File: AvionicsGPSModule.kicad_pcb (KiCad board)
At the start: 4 copper layers, 60 x 56.1 mm, 45 parts, among them P1 MC311D, Q1 AO3400A, Q2 AO3400A, U1 RP2040, U2 AP2112K-3.3, U3 L80-R, U4 W25Q128JVS, X1 ABM8-272-T3

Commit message: added CAN Transciever
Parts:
- added C16: 100nF, PCM_JLCPCB:C_0402, F.Cu at (130.6, 93.9)
- added R10: 1k, Resistor_SMD:R_0402_1005Metric, F.Cu at (128.7, 103.6)
- added R14: 120Ω, PCM_JLCPCB:R_0402, F.Cu at (130.5, 103.2)
- added R9: 1k, Resistor_SMD:R_0402_1005Metric, F.Cu at (126.5, 101.6)
- added U5: SN65HVD230DR, PCM_JLCPCB:SOIC-8_L4.9-W3.9-P1.27-LS6.0-BL, F.Cu at (130.7, 98.3)
- moved G*** 1.94 mm to (121.2, 98.2)
- moved C1 1.13 mm to (142.9, 102.8)
- moved U2 1.07 mm to (143.5, 105.4)
- moved C2 1.05 mm to (144.6, 108.4)
- moved C5 0.56 mm to (143.4, 99.4), turned to -90 degrees
- moved D5 0.13 mm to (137.9, 99.1)
- moved C12 0.11 mm to (153.9, 99.6)
- moved C7 0.10 mm to (153.9, 96.0)
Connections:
- net /RX renamed /UART_RX0
- net /TX renamed /UART_TX0
- REF** pad 2: (no net) -> /CANL
- REF** pad 3: (no net) -> /CANH
- U1 pad 11: unconnected-(U1-GPIO8-Pad11) -> /UART_TX1
- U1 pad 12: unconnected-(U1-GPIO9-Pad12) -> /UART_RX1
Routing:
- net GND: track 75.5 -> 104.3 mm, vias 29 -> 33
- net /CANH: track 0.00 -> 22.1 mm
- net /CANL: track 0.00 -> 21.4 mm
- net /UART_RX1: track 0.00 -> 21.0 mm
- net /UART_TX1: track 0.00 -> 17.9 mm
- net Net-(U5-VREF): track 0.00 -> 4.02 mm
- net +3.3V: track 88.0 -> 90.3 mm, vias 5 -> 3
- net /QSPI_SS: track 19.1 -> 19.7 mm
- net +5V: track 68.2 -> 67.6 mm
- net /QSPI_SD1: track 14.7 -> 15.2 mm
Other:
- board text removed: "GPS"
- board text removed: "MCU"

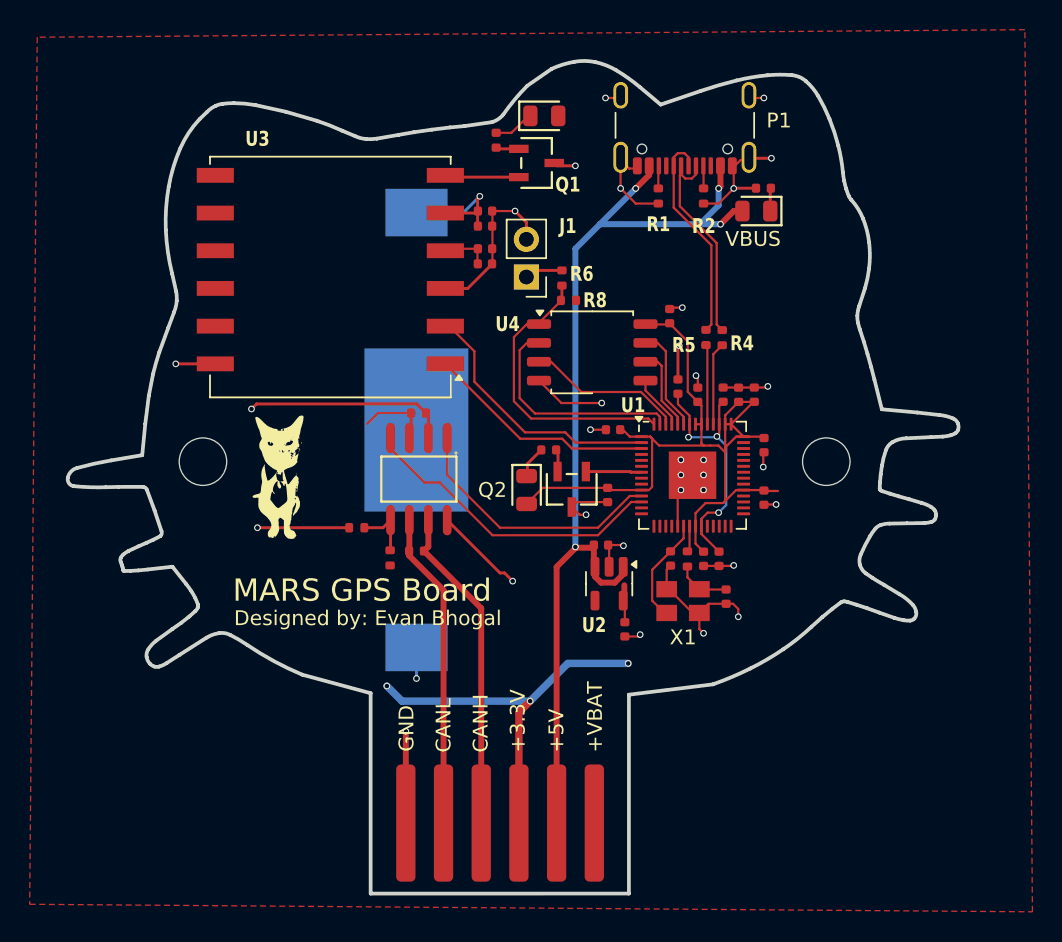
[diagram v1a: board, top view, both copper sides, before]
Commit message: Added CAN Transciever and CAN Controller
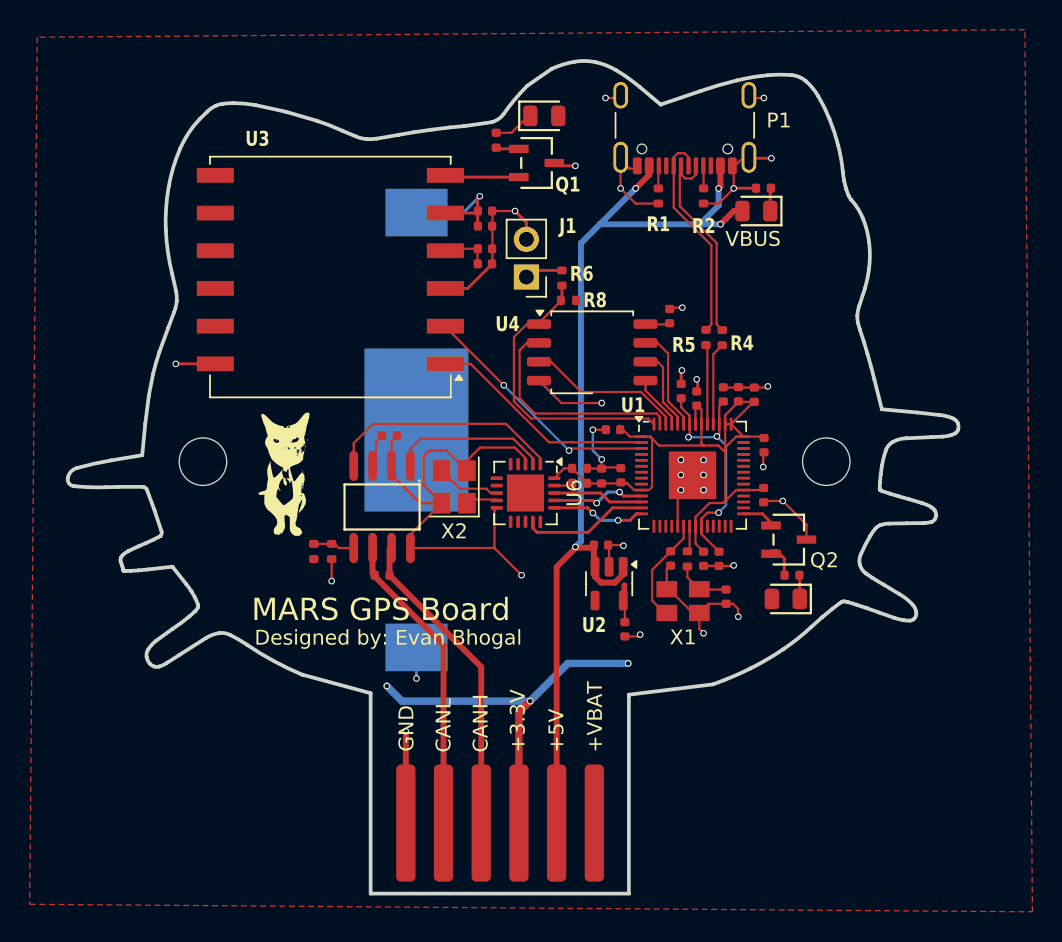
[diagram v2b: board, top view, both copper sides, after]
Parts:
- removed C4: 100n, Library:C_0402_1005Metric
- added C24: 100nF, PCM_JLCPCB:C_0402, F.Cu at (141.5, 97.6)
- added C25: 10nF, PCM_JLCPCB:C_0402, F.Cu at (143.0, 98.1)
- added C6: 100n, Library:C_0402_1005Metric, F.Cu at (151.2, 92.6)
- added R13: 5.1kΩ, PCM_JLCPCB:R_0402, F.Cu at (141.5, 98.6)
- added U6: MCP2515_I/ML, Package_DFN_QFN:QFN-20-1EP_4x4mm_P0.5mm_EP2.5x2.5mm, F.Cu at (137.9, 99.3)
- added X2: XTM32020000QT00351001, Crystal:Crystal_SMD_3225-4Pin_3.2x2.5mm, F.Cu at (133.1, 98.8)
- C11: value 100n -> 1.0u
- moved D5 18.9 mm to (155.4, 106.4), turned to 180 degrees
- moved R12 18.4 mm to (155.8, 104.8), turned to 180 degrees
- moved Q2 15.0 mm to (155.6, 102.4), turned to -90 degrees
- moved C5 11.1 mm to (152.2, 92.6), turned to 90 degrees
- moved C10 9.61 mm to (144.3, 98.1)
- moved R10 5.16 mm to (123.6, 103.2)
- moved U5 3.11 mm to (128.2, 100.2)
- moved R14 2.84 mm to (128.2, 104.8)
- moved C16 2.48 mm to (128.7, 95.4)
- moved R9 2.33 mm to (124.8, 103.2), turned to -90 degrees
- moved G*** 0.45 mm to (121.6, 98.0)
- moved C6 0.37 mm to (148.4, 92.4)
- moved C11 0.26 mm to (149.4, 92.9)
- moved C12 0.17 mm to (153.9, 99.4)
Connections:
- U1 pad 11: /UART_TX1 -> /SPI1 RX
- U1 pad 12: /UART_RX1 -> /SPI1 CSn
- U1 pad 13: unconnected-(U1-GPIO10-Pad13) -> /SPI1 SCK
- U1 pad 14: unconnected-(U1-GPIO11-Pad14) -> /SPI1 TX
- U1 pad 2: /UART_TX0 -> /MCU_TX0
- U1 pad 29: unconnected-(U1-GPIO18-Pad29) -> Net-(Q2-D)
- U1 pad 3: /UART_RX0 -> /MCU_RX0
- U1 pad 7: Net-(Q2-D) -> unconnected-(U1-GPIO5-Pad7)
- U3 pad 1: /UART_RX0 -> /MCU_TX0
- U3 pad 2: /UART_TX0 -> /MCU_RX0
- U5 pad 1: /UART_TX1 -> /TRNS_TXD
- U5 pad 4: /UART_RX1 -> /TRNS_RXD
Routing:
- net /UART_RX1: track 21.0 -> 0.00 mm
- net /UART_TX1: track 17.9 -> 0.00 mm
- net /UART_TX0: track 17.7 -> 0.00 mm
- net /MCU_RX0: track 0.00 -> 16.8 mm, vias 0 -> 2
- net /TRNS_RXD: track 0.00 -> 16.0 mm
- net /UART_RX0: track 15.6 -> 0.00 mm
- net /MCU_TX0: track 0.00 -> 15.4 mm
- net GND: track 104.3 -> 117.8 mm, vias 33 -> 32
- net +3.3V: track 90.3 -> 79.2 mm
- net /TRNS_TXD: track 0.00 -> 10.6 mm
- net /SPI1 SCK: track 0.00 -> 8.55 mm
- net /SPI1 TX: track 0.00 -> 6.41 mm, vias 0 -> 2
- net /SPI1 RX: track 0.00 -> 6.37 mm, vias 0 -> 2
- net /SPI1 CSn: track 0.00 -> 6.13 mm
- net Net-(U6-OSC2): track 0.00 -> 4.34 mm
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
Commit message: Respecced crystal, added Schottky Diode
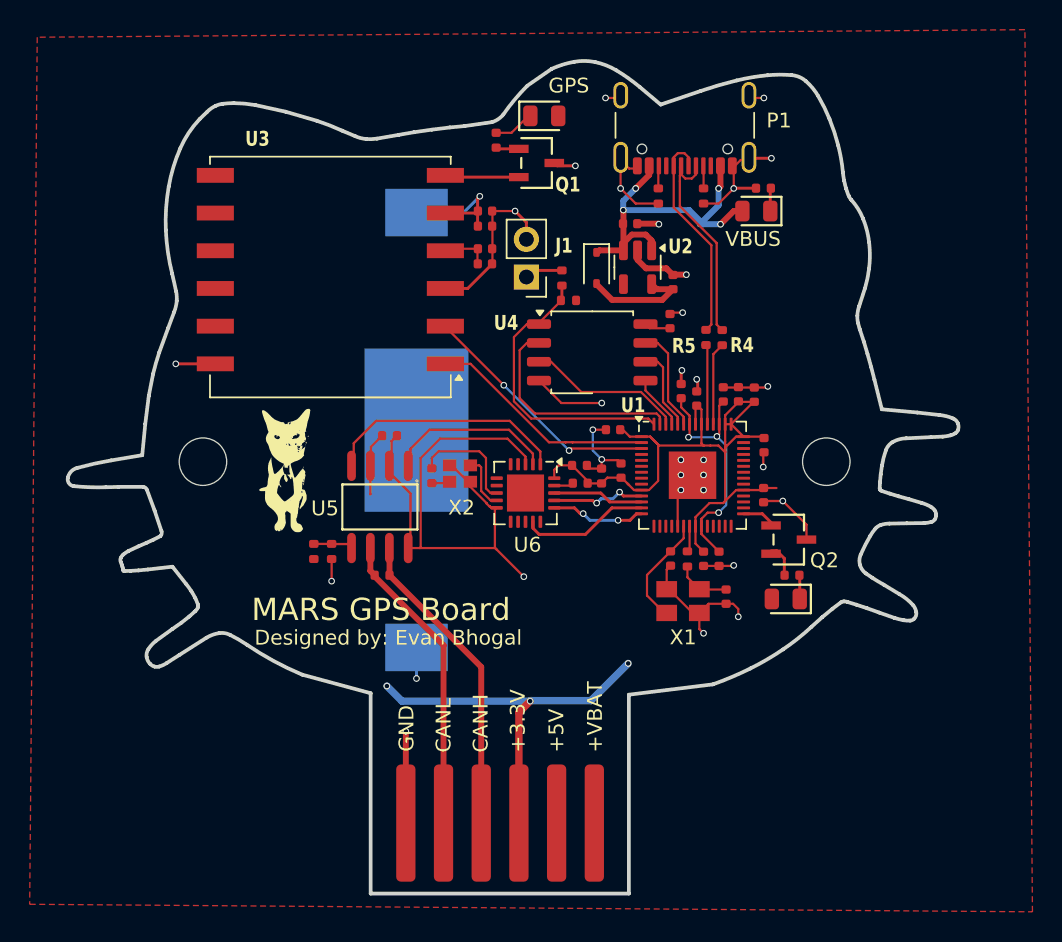
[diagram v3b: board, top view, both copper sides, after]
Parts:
- added D3: CUS10S30,H3F, Diode_SMD:D_SOD-323, F.Cu at (142.7, 84.1)
- added R15: 1kΩ, PCM_JLCPCB:R_0402, F.Cu at (131.6, 98.1)
- X2: value XTM32020000QT00351001 -> 20 MHz; footprint Crystal:Crystal_SMD_3225-4Pin_3.2x2.5mm -> Crystal:Crystal_SMD_2016-4Pin_2.0x1.6mm
- moved C2 23.6 mm to (147.8, 85.0), turned to 90 degrees
- moved C1 21.7 mm to (144.9, 81.1)
- moved U2 21.4 mm to (145.4, 84.0)
- moved X2 0.98 mm to (133.4, 98.0), turned to 180 degrees
- moved C18 0.34 mm to (147.6, 87.7)
- moved C10 0.32 mm to (144.3, 97.8)
- moved G*** 0.25 mm to (121.7, 97.8)
- moved C24 0.20 mm to (141.5, 97.4)
- moved U5 0.15 mm to (128.1, 100.2)
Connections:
- REF** pad 5: +5V -> (no net)
- X2 pad 3: Net-(U6-OSC2) -> Net-(C22-Pad1)
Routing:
- net +5V: track 67.6 -> 25.3 mm
- net +3.3V: track 79.2 -> 88.1 mm
- net GND: track 117.8 -> 124.5 mm
- net Net-(U6-OSC2): track 4.34 -> 7.63 mm
- net Net-(U6-OSC1): track 1.90 -> 3.69 mm
- net Net-(C22-Pad1): track 0.00 -> 1.24 mm
- net /TRNS_TXD: track 10.6 -> 11.3 mm
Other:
- board text added: "GPS"

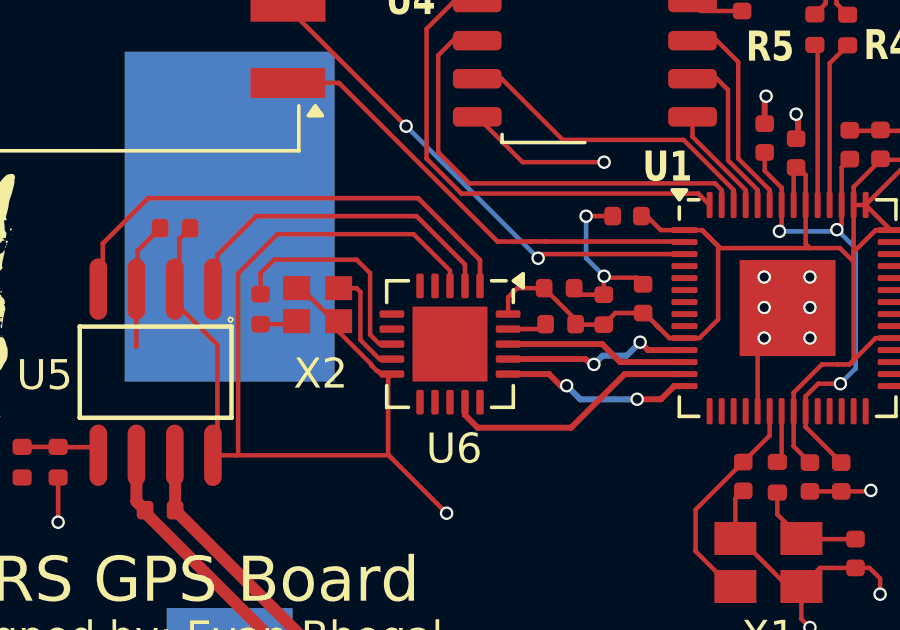
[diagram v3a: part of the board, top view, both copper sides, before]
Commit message: Fixed Mounting Pad for CAN Controller
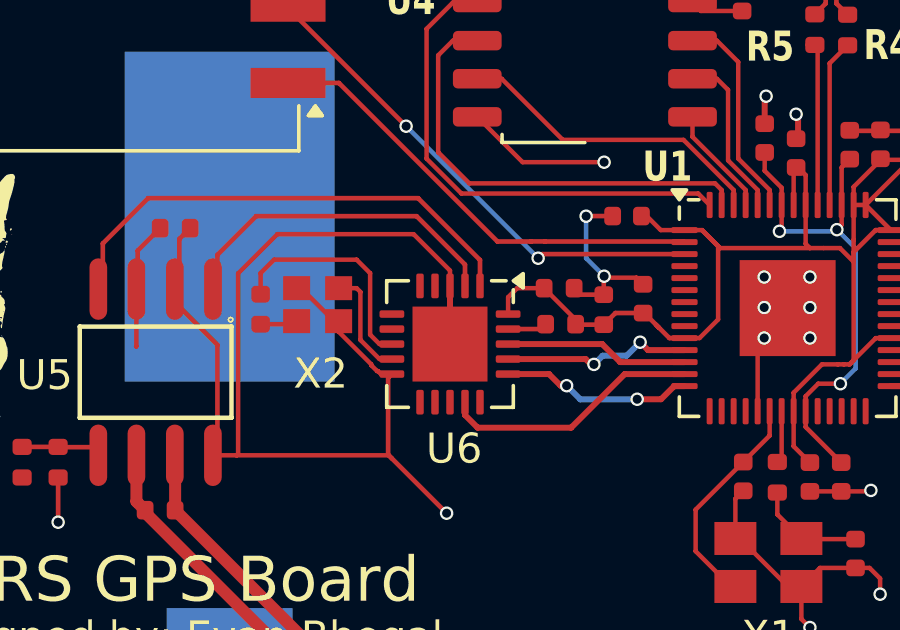
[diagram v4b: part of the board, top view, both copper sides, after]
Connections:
- U6 pad 21: (no net) -> GND
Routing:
- net GND: track 124.5 -> 126.5 mm
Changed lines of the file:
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@@
 			(property pad_prop_heatsink)
 			(layers "F.Cu" "F.Mask")
+			(net 2 "GND")
 			(zone_connect 2)
 		)
@@
 		(layer "F.Cu")
 		(net 2)
+	)
+	(segment
+		(start 137.8625 99.2625)
+		(end 137.8625 97.325)
+		(width 0.2)
+		(layer "F.Cu")
+		(net 2)

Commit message: Fixed MOSFET Driver
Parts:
- moved R12 4.21 mm to (158.4, 101.5)
- moved D5 4.00 mm to (158.4, 103.8), turned to -90 degrees
- moved Q2 0.53 mm to (155.4, 102.9), turned to 180 degrees
- moved G*** 0.20 mm to (121.8, 97.8)
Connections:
- R12 pad 2: Net-(Q2-G) -> Net-(Q2-D)
- U1 pad 29: Net-(Q2-D) -> Net-(Q2-G)
- U6 pad 21: GND -> (no net)
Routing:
- net GND: track 126.5 -> 125.0 mm, vias 32 -> 33
